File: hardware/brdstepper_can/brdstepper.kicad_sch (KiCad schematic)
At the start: 94 parts, among them J1 USB-C, J2 VM / GND / EN, J3 MOTOR, J4 SMART-SERIAL, J5 CAN, J6 CAN, J7 SWD, U1 STM32G473CEU6, U2 DRV8876RGTR, U3 DRV8876RGTR, U4 AS5047P-ATSM, U5 TLV75533PDBVR, U6 TPS560430XDBVR, U7 USBLC6-2SC6, U8 SN65HVD30DR, U9 TCAN1044VDR, Y1 8MHz

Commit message: brdstepper: split into serial and CAN boards, 0603 passives (WIP, not routed)
- hardware/brdstepper_common: shared parts/board definitions built per
  variant; brdstepper_mesa (A, smart-serial) and brdstepper_can (B, CAN)
  each fit only their own interface parts, MCU pins of the other
  interface left open, HWID divider per variant.
- 0402 resistors and capacitors become 0603; power capacitors stay larger.
- kigen place: GAP_MAX bisects the largest courtyard gap that still
  places every part (0603 on 28 x 28 mm only just fits: gap ~0).
- kigen route: DSN export, BrdRoute, SES import, zone fill (untested end
  to end: first router run still going).

Not done yet: routing on 4 layers, READMEs/BOMs/renders refresh, DEBUGNOTES.

Co-Authored-By: Claude Sonnet 5.5 <noreply@anthropic.com>
Claude-Session: https://claude.ai/code/session_017CSpK2B8oMBAmr39Kq1RSC
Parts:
- removed C38: 100n, Capacitor_SMD:C_0402_1005Metric, symbol Device:C
- removed D3: BAT54WS, Diode_SMD:D_SOD-323, symbol Device:D_Schottky
- removed J4: SMART-SERIAL, Connector_JST:JST_GH_SM06B-GHS-TB_1x06-1MP_P1.25mm_Horizontal, symbol Connector_Generic_MountingPin:Conn_01x06_MountingPin
- removed R20: 120, Resistor_SMD:R_0402_1005Metric, symbol Device:R
- removed U8: SN65HVD30DR, Package_SO:SOIC-8_3.9x4.9mm_P1.27mm, symbol Interface_UART:MAX3490xSA
- C10, C11, C12, C13, C14, C15, C16, C17, C18, C19, C20, C22, C23, C25, C26, C27, C29, C30, C31, C32, C33, C34, C36, C37, C39, C4, C40, C5, C8, C9: footprint Capacitor_SMD:C_0402_1005Metric -> Capacitor_SMD:C_0603_1608Metric
- R1, R10, R11, R12, R13, R14, R15, R16, R17, R18, R19, R2, R21, R3, R4, R5, R6, R7, R9: footprint Resistor_SMD:R_0402_1005Metric -> Resistor_SMD:R_0603_1608Metric
- R8: footprint Resistor_SMD:R_0402_1005Metric -> Resistor_SMD:R_0603_1608Metric; Note §6 HWID: A 0 Ω, B 10k -> §6 HWID: variant B, with R7 10k: 1.65 V
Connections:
- net SS_RX: no longer names the net of U1.45 (PB7)
- net SS_TX: no longer names the net of U1.44 (PB6)
- no-connect marks 19 -> 21
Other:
- note added: "USB-C, CAN, mounting"
- note added: "brdstepper B: STM32G473 + AS5047P + 2x DRV8876, 28 x 28 mm on the back of a NEMA11 motor. Connections are by net name (net labels): docs/brdstepper_hw.md is the reference. Variant B: U9/J5/J6/JP1, CAN."
- note removed: "USB-C, smart-serial (variant A), CAN (variant B), mounting"
- note removed: "brdstepper: STM32G473 + AS5047P + 2x DRV8876, 28 x 28 mm on the back of a NEMA11 motor. Connections are by net name (net labels): docs/brdstepper_hw.md is the reference. Variant A fits U8/J4 (smart-serial to a Mesa card), variant B U9/J5/J6/JP1 (CAN)."
- title: brdstepper: closed-loop NEMA11 stepper drive -> brdstepper: closed-loop NEMA11 stepper drive, CAN
- moved on the sheet: C10, C11, C12, C13, C14, C23, C24, C25, C26, C27, C28, C29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

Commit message: brdstepper: USB and SWD as test pads, motor pads on the edge, plane fanout (WIP)
- USB-C connector, its CC/shield parts and ESD chip replaced by four test
  pads (5V, D+, D-, GND) on both boards; SWD header by five test pads.
- Motor pads J3 fixed on the north edge of both boards.
- All fixed parts (the encoder on the shaft axis, holes, edge connectors)
  are locked in the generated board.
- Placement is much looser without the two connectors: serial board
  courtyard gap 0.30 mm.
- kigen route: loads a bare board (pcbnew 7 crashes when tracks are
  removed), GND plane fanout (a via + stub per SMD pad, vias in the MCU's
  exposed pad), In1 hidden from the router, router exit code ignored when
  a session was written.
- DEBUGNOTES: headless pcbnew gotchas.

Needs the BrdRoute plane-net change (not yet committed there); boards are
a routing snapshot, not complete.

Co-Authored-By: Claude Sonnet 5.5 <noreply@anthropic.com>
Claude-Session: https://claude.ai/code/session_017CSpK2B8oMBAmr39Kq1RSC
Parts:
- removed C37: 4.7n, Capacitor_SMD:C_0603_1608Metric, symbol Device:C
- removed J1: USB-C, Connector_USB:USB_C_Receptacle_GCT_USB4105-xx-A_16P_TopMnt_Horizontal, symbol Connector:USB_C_Receptacle_USB2.0_16P
- removed J7: SWD, Connector_PinHeader_1.27mm:PinHeader_1x05_P1.27mm_Vertical_SMD_Pin1Left, symbol Connector_Generic:Conn_01x05
- removed R17, R18: 5.1k, Resistor_SMD:R_0603_1608Metric, symbol Device:R
- removed R19: 1M, Resistor_SMD:R_0603_1608Metric, symbol Device:R
- removed U7: USBLC6-2SC6, Package_TO_SOT_SMD:SOT-23-6, symbol Power_Protection:USBLC6-2SC6
- added TP10: USB D+, TestPoint:TestPoint_Pad_D1.0mm, symbol Connector:TestPoint
- added TP11: USB D-, TestPoint:TestPoint_Pad_D1.0mm, symbol Connector:TestPoint
- added TP12: USB GND, TestPoint:TestPoint_Pad_D1.0mm, symbol Connector:TestPoint
- added TP4: SWD 3V3, TestPoint:TestPoint_Pad_D1.0mm, symbol Connector:TestPoint
- added TP5: SWDIO, TestPoint:TestPoint_Pad_D1.0mm, symbol Connector:TestPoint
- added TP6: NRST, TestPoint:TestPoint_Pad_D1.0mm, symbol Connector:TestPoint
- added TP7: SWCLK, TestPoint:TestPoint_Pad_D1.0mm, symbol Connector:TestPoint
- added TP8: SWD GND, TestPoint:TestPoint_Pad_D1.0mm, symbol Connector:TestPoint
- added TP9: USB 5V, TestPoint:TestPoint_Pad_D1.0mm, symbol Connector:TestPoint
- J3: Note A+ A- B+ B-: solder pads for the motor leads (§4.7 allows p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 -> A+ A- B+ B-: solder pads for the motor leads, on the board 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
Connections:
- net 3V3: now also TP4.1
- net 5V_USB: now also TP9.1
- net GND: now also TP12.1, TP8.1
- net NRST: now also TP6.1
- net SWCLK: now also TP7.1
- net SWDIO: now also TP5.1
- net USB_DM: now also TP11.1
- net USB_DP: now also TP10.1
- no-connect marks 21 -> 19
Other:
- note added: "USB pads, CAN, mounting"
- note removed: "USB-C, CAN, mounting"
- moved on the sheet: C39, C40, H1, H2, H3, H4, J5, J6, JP1, R10, R21, TH1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

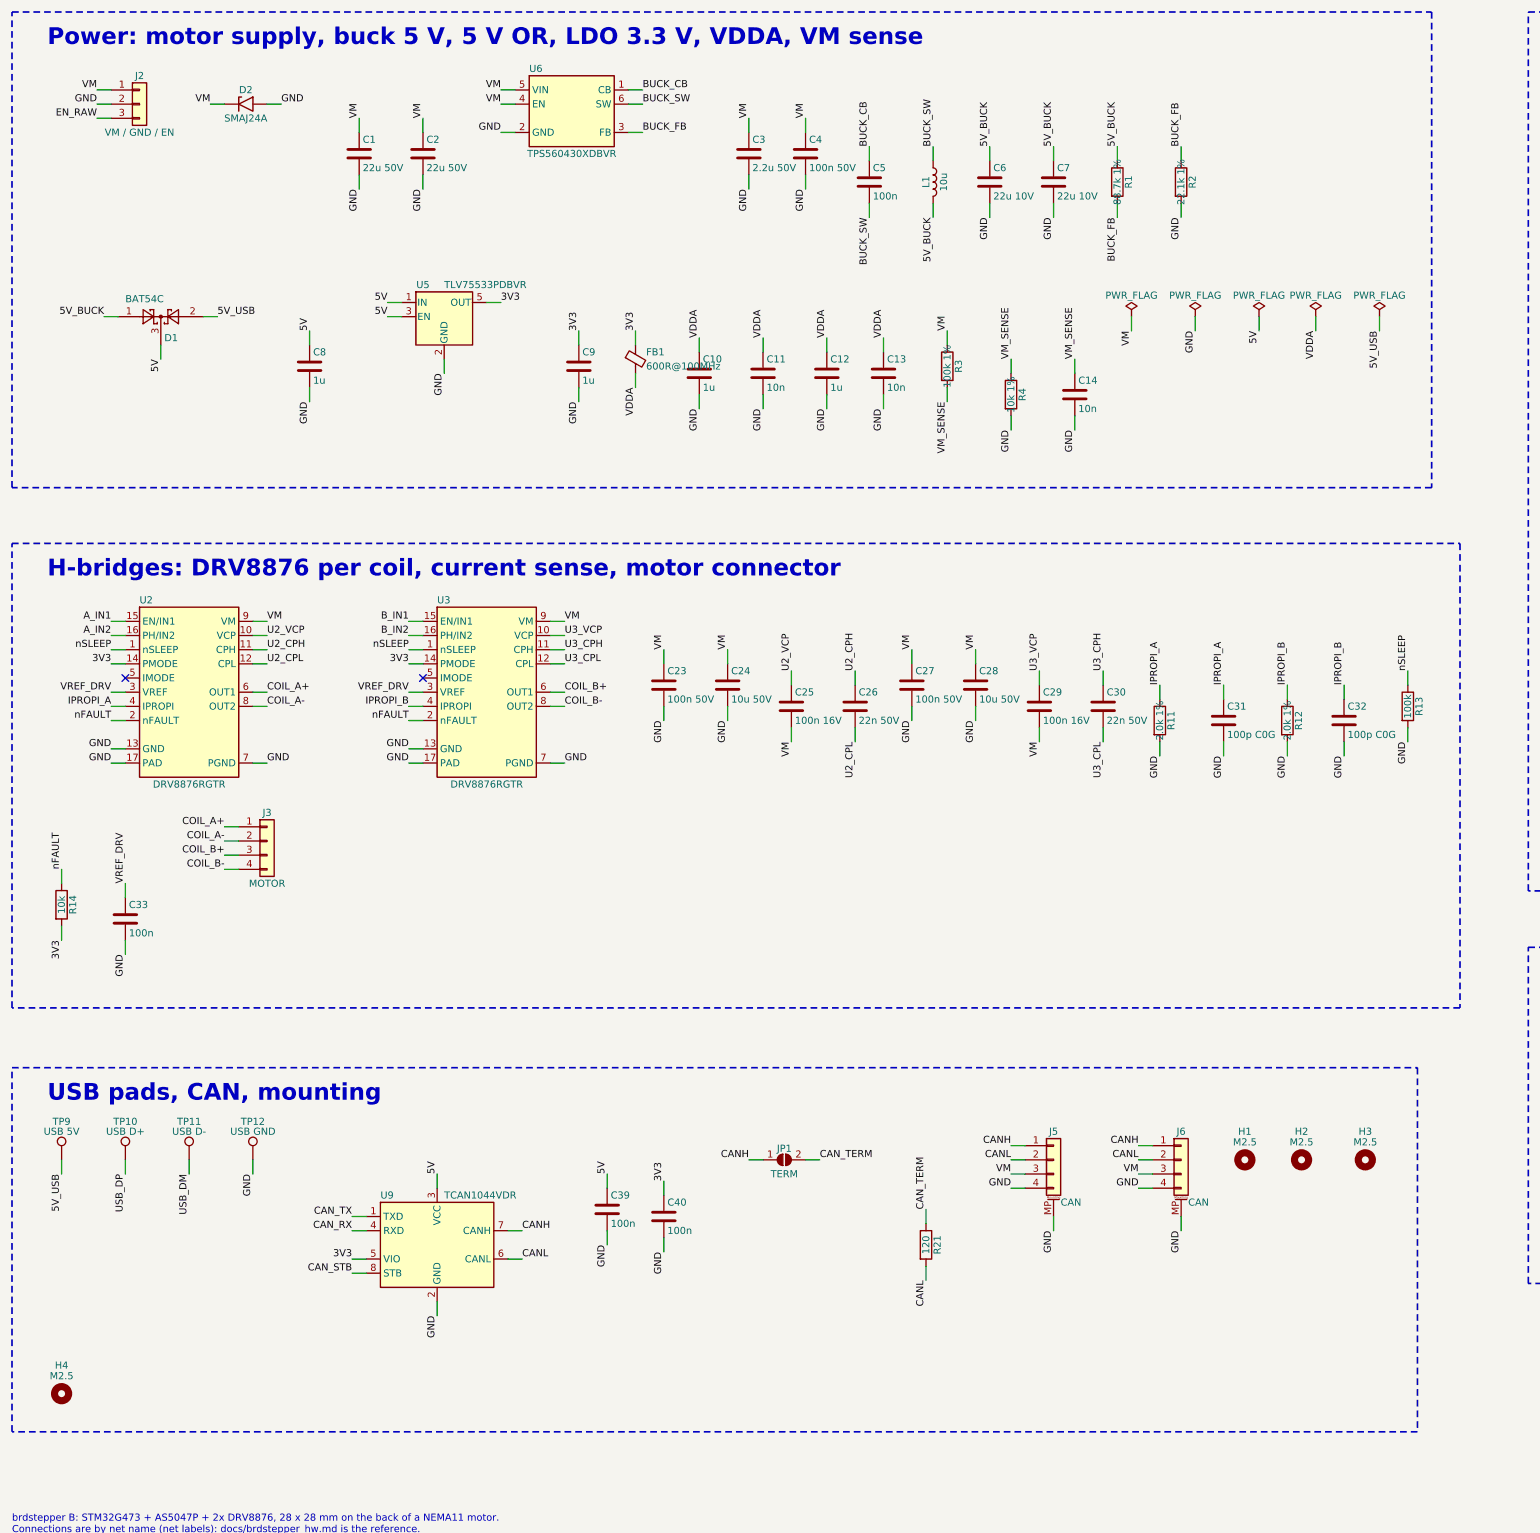
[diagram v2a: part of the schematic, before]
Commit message: brdstepper: drop J2, supply and enable on the signal connectors (WIP)
- Serial board: J4 becomes 8-pin GH (adds VM, EN to TX+/-, RX+/-, 5 V, GND).
- CAN board: J5/J6 become 5-pin GH (adds EN to CANH, CANL, VM, GND).
- No separate supply connector: nothing with supply current beside the
  encoder any more. GH is 1 A per contact (flagged in the BOM notes).

Schematics regenerated; the .kicad_pcb files in this commit are from
before the change and are being re-placed.

Co-Authored-By: Claude Sonnet 5.5 <noreply@anthropic.com>
Claude-Session: https://claude.ai/code/session_017CSpK2B8oMBAmr39Kq1RSC
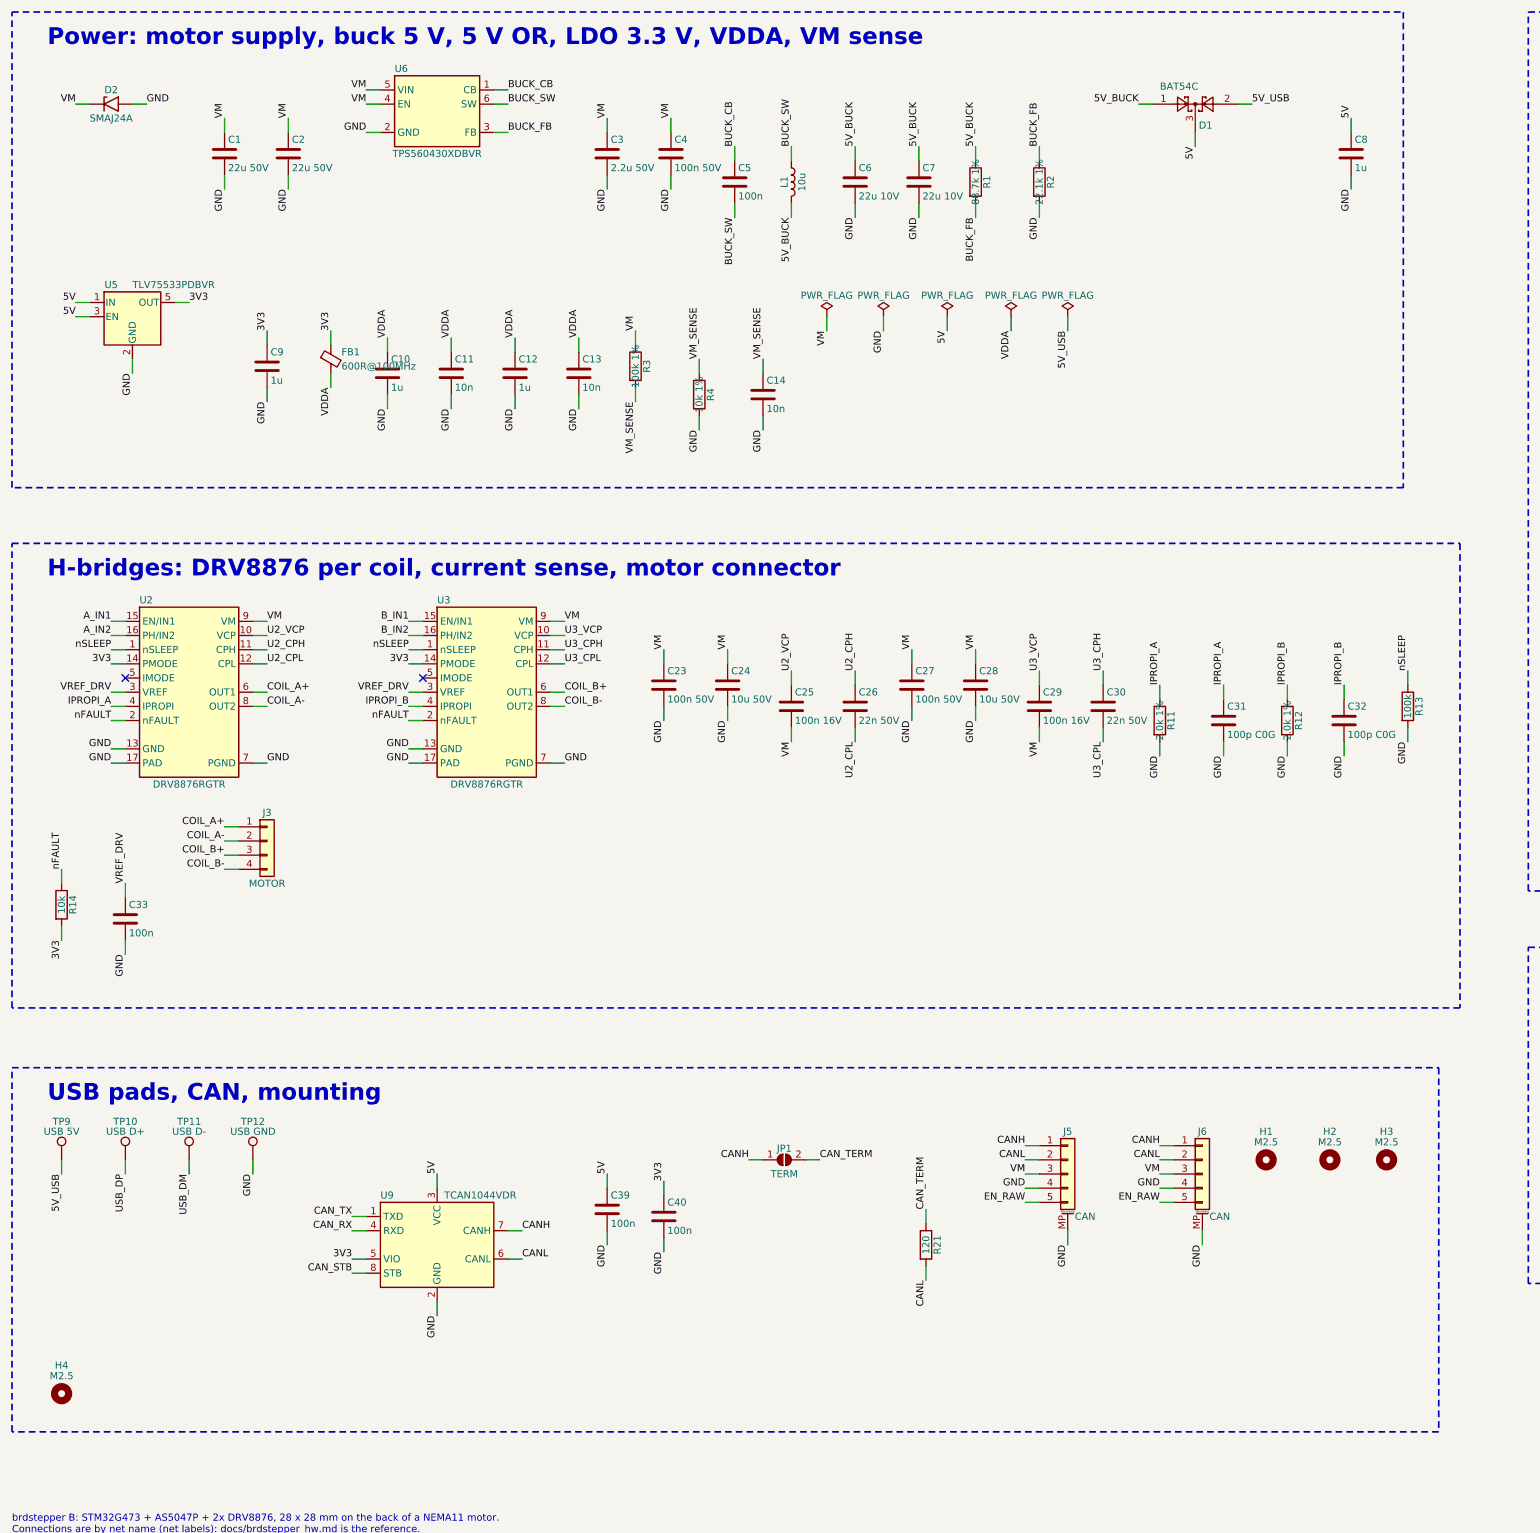
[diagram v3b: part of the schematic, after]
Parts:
- removed J2: VM / GND / EN, Connector_JST:JST_XH_B3B-XH-A_1x03_P2.50mm_Vertical, symbol Connector_Generic:Conn_01x03
- J5: footprint Connector_JST:JST_GH_SM04B-GHS-TB_1x04-1MP_P1.25mm_Horizontal -> Connector_JST:JST_GH_SM05B-GHS-TB_1x05-1MP_P1.25mm_Horizontal; symbol Connector_Generic_MountingPin:Conn_01x04_MountingPin -> Connector_Generic_MountingPin:Conn_01x05_MountingPin; Note variant B -> variant B; VM is also the motor supply, EN the enable / est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
- J6: footprint Connector_JST:JST_GH_SM04B-GHS-TB_1x04-1MP_P1.25mm_Horizontal -> Connector_JST:JST_GH_SM05B-GHS-TB_1x05-1MP_P1.25mm_Horizontal; symbol Connector_Generic_MountingPin:Conn_01x04_MountingPin -> Connector_Generic_MountingPin:Conn_01x05_MountingPin; Note variant B, daisy chain -> variant B, daisy chain; VM is also the motor supply, EN the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
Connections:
- net EN_RAW: now also J5.5 (Pin_5), J6.5 (Pin_5)
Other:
- moved on the sheet: C1, C10, C11, C12, C13, C14, C2, C3, C4, C5, C6, C7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
